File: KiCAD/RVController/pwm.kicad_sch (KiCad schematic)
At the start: 2 parts, among them Q1 EPC2014C

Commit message: Done?
Routed, etc. Exported STEP.
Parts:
- Q1: footprint TRANS_EPC2014C -> Footprints:TRANS_EPC2014C
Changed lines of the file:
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@@
     (property "Reference" "Q1" (id 0) (at 90.17 81.28 0))
     (property "Value" "EPC2014C" (id 1) (at 92.71 83.82 0))
-    (property "Footprint" "TRANS_EPC2014C" (id 2) (at 78.74 80.01 0)
+    (property "Footprint" "Footprints:TRANS_EPC2014C" (id 2) (at 78.74 80.01 0)
       (effects (font (size 1.27 1.27)) (justify left bottom) hide)
     )

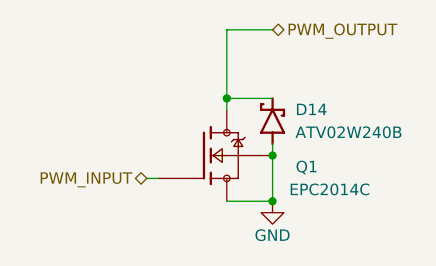
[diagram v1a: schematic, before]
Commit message: Updated to SMD socket
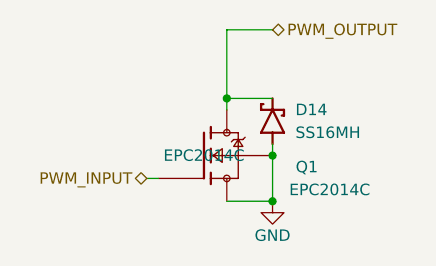
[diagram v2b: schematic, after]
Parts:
- D14: value ATV02W240B -> SS16MH; footprint Footprints:SODFL2512X73N -> Diode_SMD:D_SOD-123FAC; PN ATV02W240B -> SS16MH
- Q1: footprint Footprints:TRANS_EPC2014C -> TRANS_EPC2014C; PN (none) -> EPC2014C
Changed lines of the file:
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@@
     (property "Reference" "Q1" (id 0) (at 90.17 81.28 0))
     (property "Value" "EPC2014C" (id 1) (at 92.71 83.82 0))
-    (property "Footprint" "Footprints:TRANS_EPC2014C" (id 2) (at 78.74 80.01 0)
+    (property "Footprint" "TRANS_EPC2014C" (id 2) (at 78.74 80.01 0)
       (effects (font (size 1.27 1.27)) (justify left bottom) hide)
     )
@@
       (effects (font (size 1.27 1.27)) (justify left bottom) hide)
     )
+    (property "PN" "EPC2014C" (id 8) (at 78.74 80.01 0))
     (pin "1")
     (pin "2")
@@
       (effects (font (size 1.27 1.27)) (justify right))
     )
-    (property "Value" "ATV02W240B" (id 1) (at 88.9 77.4699 90)
+    (property "Value" "SS16MH" (id 1) (at 88.9 77.4699 90)
       (effects (font (size 1.27 1.27)) (justify right))
     )
-    (property "Footprint" "Footprints:SODFL2512X73N" (id 2) (at 86.36 76.2 0)
+    (property "Footprint" "Diode_SMD:D_SOD-123FAC" (id 2) (at 86.36 76.2 0)
       (effects (font (size 1.27 1.27)) (justify left bottom) hide)
     )
@@
       (effects (font (size 1.27 1.27)) (justify left bottom) hide)
     )
-    (property "PN" "ATV02W240B" (id 8) (at 86.36 76.2 90)
+    (property "PN" "SS16MH" (id 8) (at 86.36 76.2 90)
       (effects (font (size 1.27 1.27)) hide)
     )

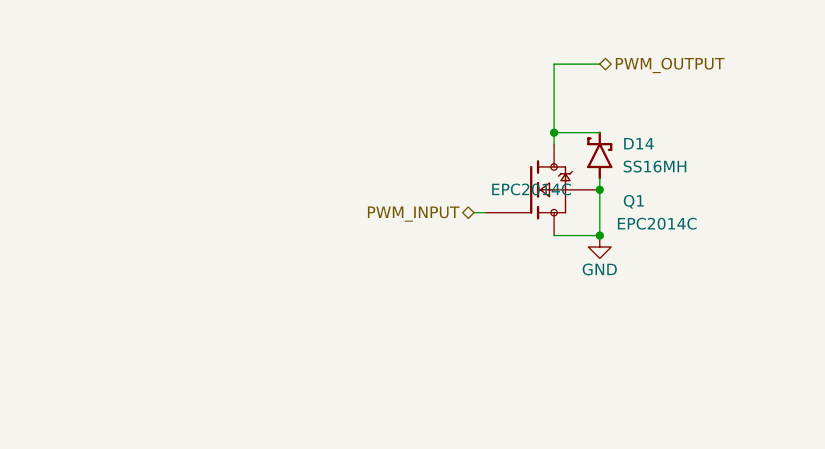
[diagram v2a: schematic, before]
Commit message: Updates to new parts, routed
Changed to alternative FETs, Schottky diodes, TVS, etc. Ready for production
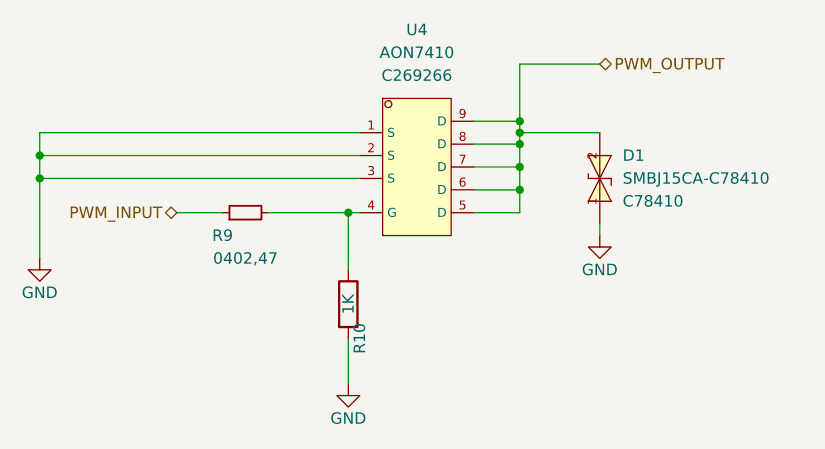
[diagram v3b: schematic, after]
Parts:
- removed D14: SS16MH, Diode_SMD:D_SOD-123FAC, symbol Schematic:SS16MH
- removed Q1: EPC2014C, TRANS_EPC2014C, symbol Schematic:EPC2014C
- added D1: SMBJ15CA-C78410, Footprints:SMB_L4.6-W3.6-LS5.3-BI, symbol Schematic:SMBJ15CA-C78410
- added R10: 1K, Resistor_SMD:R_0805_2012Metric, symbol Device:R
- added R9: 0402,47, Resistor_SMD:R_0402_1005Metric, symbol jlcpcb-basic-resistor:0402,47
- added U4: AON7410, Footprints:DFN-8_L3.0-W3.0-P0.65-BL, symbol Schematic:AON7410
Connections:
- net GND: now also D1.1, R10.2, U4.1 (S), U4.2 (S), U4.3 (S)
- net PWM_INPUT: now also R9.1
- net PWM_OUTPUT: now also D1.2, U4.5 (D), U4.6 (D), U4.7 (D), U4.8 (D), U4.9 (D)
- new net: R10.1, R9.2, U4.4 (G)
